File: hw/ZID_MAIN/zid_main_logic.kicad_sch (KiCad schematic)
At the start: 81 parts, among them J1 Conn_01x02_Pin_2.54mm, J2 Conn_02x05_2.54mm, J3 Conn_02x05_2.54mm, J4 Conn_02x05_PINHDR_2.54mm, J5 HDR 1x04 Socket, J6 Conn_02x03_Odd_Even, J7 Conn_01x03, M1 WS-RP2040-Zero, SW1 SW_Push, SW2 SW_DIP_x02, U1 74HCT161, U10 74FCT2245, U11 SST39SF010, U12 AS7C1024B-10J, U13 74FCT541C, U14 74AHCT244, U15 74FCT257T, U16 74HCT166, U17 74HCT166, U18 74LVC245, U19 74LVC125AS, U2 74FCT541C, U20 24LC32, U21 ATF1504AS-44T, U22 74AHCT1G125, U23 74LVC273, U25 74LVC2G04, U26 74LVC2G04-AES, U3 74FCT541C, U4 MIC2775, U6 Z80 C20MHz-PLCC, U7 ATF1508AS, U8 74FCT2245, U9 74FCT2245

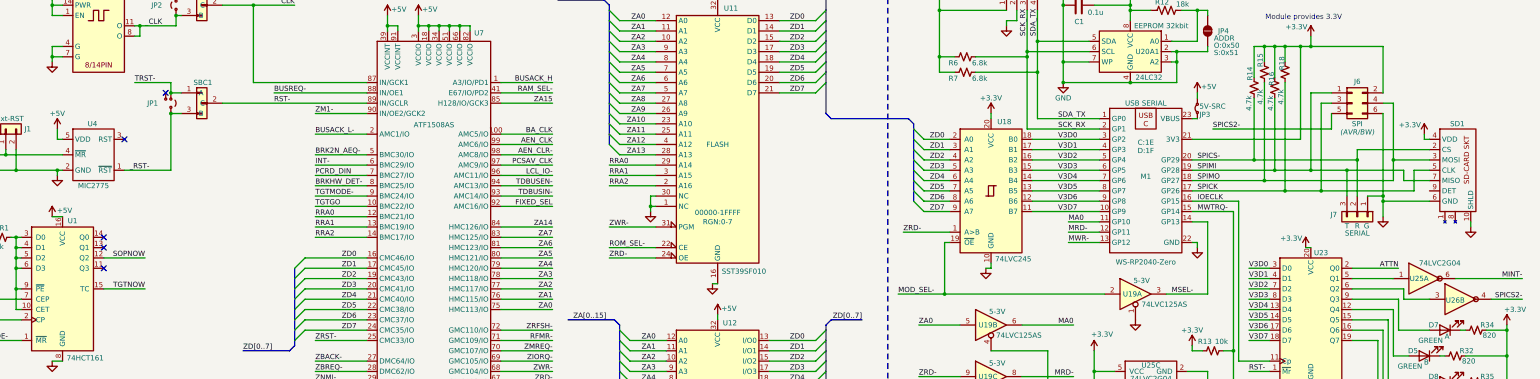
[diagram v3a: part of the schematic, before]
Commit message: Footprints assigned
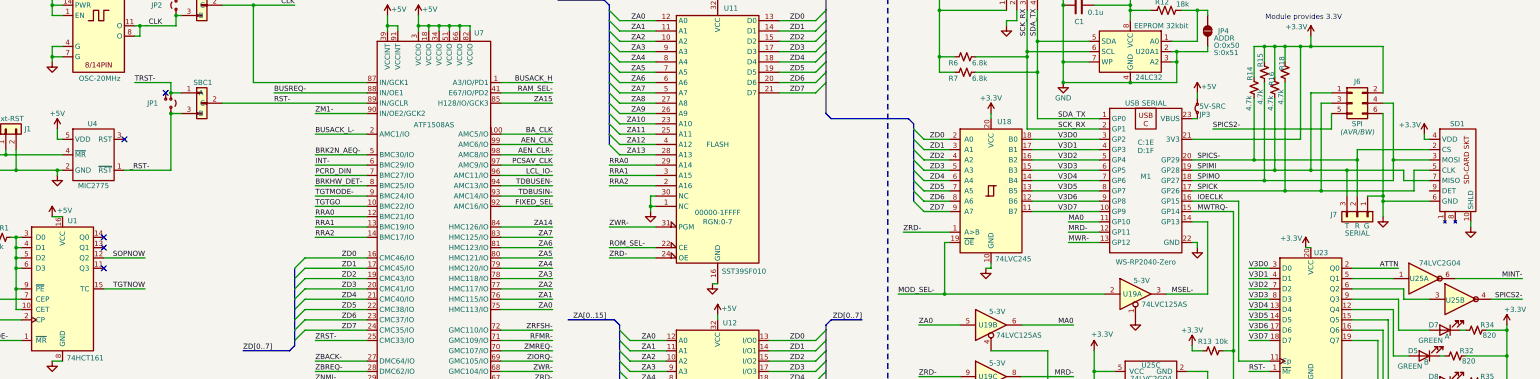
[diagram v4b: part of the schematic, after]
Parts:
- D5, D7: value LED RED -> LED GREEN; footprint LED_THT:LED_D3.0mm -> LED_SMD:LED_0805_2012Metric_Pad1.15x1.40mm_HandSolder
- D6, D8: value LED RED -> LED YELLOW; footprint LED_THT:LED_D3.0mm -> LED_SMD:LED_0805_2012Metric_Pad1.15x1.40mm_HandSolder
- D9: footprint LED_THT:LED_D3.0mm -> LED_SMD:LED_0805_2012Metric_Pad1.15x1.40mm_HandSolder
- J1: footprint (none) -> Connector_PinHeader_2.54mm:PinHeader_1x02_P2.54mm_Vertical
- J2, J3: footprint (none) -> Connector_PinHeader_2.54mm:PinHeader_2x05_P2.54mm_Vertical
- J4: footprint (none) -> Connector_IDC:IDC-Header_2x05_P2.54mm_Vertical
- J6: footprint (none) -> Connector_IDC:IDC-Header_2x03_P2.54mm_Vertical
- J7: footprint (none) -> Connector_PinHeader_2.54mm:PinHeader_1x03_P2.54mm_Vertical
- JP1: footprint (none) -> Connector_PinHeader_2.00mm:PinHeader_1x03_P2.00mm_Vertical
- JP2, JP3: footprint (none) -> Connector_PinHeader_2.00mm:PinHeader_1x02_P2.00mm_Vertical
- JP4: footprint (none) -> Jumper:SolderJumper-2_P1.3mm_Open_RoundedPad1.0x1.5mm
- R1, R4: footprint (none) -> Resistor_SMD:R_0805_2012Metric
- R12: footprint Resistor_SMD:R_0805_2012Metric_Pad1.20x1.40mm_HandSolder -> Resistor_SMD:R_0805_2012Metric
- SD1: value ~ -> SD-CARD Socket; footprint (none) -> AES_Library:AES-SDCard-GCT_MEM2075-00-140-01-A
- SW1: footprint (none) -> AES_Library:AES-SW_PUSH_SMD_1P1T_NO_6x6mm
- SW2: footprint (none) -> Button_Switch_THT:SW_DIP_SPSTx02_Piano_CTS_Series194-2MSTN_W7.62mm_P2.54mm
- TP1, TP2, TP3, TP4, TP5, TP6: footprint (none) -> Connector_PinHeader_2.54mm:PinHeader_1x01_P2.54mm_Vertical
- U1, U16, U17: footprint (none) -> Package_SO:SOIC-16_3.9x9.9mm_P1.27mm
- U10, U13, U14, U18, U2, U23, U3, U8, U9: footprint (none) -> Package_SO:SOIC-20W_7.5x12.8mm_P1.27mm
- U11: footprint (none) -> Package_DIP:DIP-32_W15.24mm_Socket_LongPads
- U15: footprint (none) -> Package_SO:SOIC-16W_7.5x10.3mm_P1.27mm
- U22: footprint (none) -> Package_TO_SOT_SMD:SOT-23-5
- U25: renamed from U26; value 74LVC2G04-AES -> 74LVC2G04
- U5: value ~ -> OSC-20MHz
- U6: footprint Package_LCC:PLCC-44 -> Package_LCC:PLCC-44_THT-Socket
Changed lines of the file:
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@@
 			)
 		)
-		(property "Footprint" ""
+		(property "Footprint" "Connector_PinHeader_2.54mm:PinHeader_1x01_P2.54mm_Vertical"
 			(at 106.68 152.4 0)
 			(effects
@@
 			)
 		)
-		(property "Footprint" ""
+		(property "Footprint" "Resistor_SMD:R_0805_2012Metric"
 			(at 30.48 78.74 0)
 			(effects
@@
 			)
 		)
-		(property "Footprint" ""
+		(property "Footprint" "Package_SO:SOIC-20W_7.5x12.8mm_P1.27mm"
 			(at 142.24 201.93 0)
 			(effects
@@
 			)
 		)
-		(property "Footprint" ""
+		(property "Footprint" "Connector_PinHeader_2.54mm:PinHeader_1x03_P2.54mm_Vertical"
 			(at 364.49 73.66 0)
 			(effects
@@
 			)
 		)
-		(property "Footprint" "Package_LCC:PLCC-44"
+		(property "Footprint" "Package_LCC:PLCC-44_THT-Socket"
 			(at 71.12 282.448 0)
 			(effects
@@
 			)
 		)
-		(property "Footprint" ""
+		(property "Footprint" "Package_SO:SOIC-20W_7.5x12.8mm_P1.27mm"
 			(at 45.72 179.07 0)
 			(effects
@@
 			)
 		)
-		(property "Footprint" ""
+		(property "Footprint" "Connector_PinHeader_2.54mm:PinHeader_1x02_P2.54mm_Vertical"
 			(at 31.75 52.07 0)
 			(effects
@@
 			)
 		)
-		(property "Value" "LED RED"
+		(property "Value" "LED GREEN"
 			(at 380.746 105.664 0)
 			(effects
@@
 			)
 		)
-		(property "Footprint" "LED_THT:LED_D3.0mm"
+		(property "Footprint" "LED_SMD:LED_0805_2012Metric_Pad1.15x1.40mm_HandSolder"
 			(at 381 107.95 0)
 			(effects
@@
 			)
 		)
-		(property "Footprint" ""
+		(property "Footprint" "Button_Switch_THT:SW_DIP_SPSTx02_Piano_CTS_Series194-2MSTN_W7.62mm_P2.54mm"
 			(at 30.48 300.99 0)
 			(effects
@@
 			)
 		)
-		(property "Value" "LED RED"
+		(property "Value" "LED YELLOW"
 			(at 385.826 112.014 0)
 			(effects
@@
 			)
 		)
-		(property "Footprint" "LED_THT:LED_D3.0mm"
+		(property "Footprint" "LED_SMD:LED_0805_2012Metric_Pad1.15x1.40mm_HandSolder"
 			(at 386.08 114.3 0)
 			(effects
@@
 			)
 		)
-		(property "Footprint" ""
+		(property "Footprint" "Connector_PinHeader_2.54mm:PinHeader_2x05_P2.54mm_Vertical"
 			(at 171.45 285.75 0)
 			(effects
@@
 			)
 		)
-		(property "Footprint" ""
+		(property "Footprint" "Connector_IDC:IDC-Header_2x03_P2.54mm_Vertical"
 			(at 363.22 45.72 0)
 			(effects
@@
 			)
 		)
-		(property "Footprint" ""
+		(property "Footprint" "Package_SO:SOIC-16W_7.5x10.3mm_P1.27mm"
 			(at 210.82 185.42 0)
 			(effects
@@
 			)
 		)
-		(property "Value" "LED RED"
+		(property "Value" "LED GREEN"
 			(at 385.826 99.314 0)
 			(effects
@@
 			)
 		)
-		(property "Footprint" "LED_THT:LED_D3.0mm"
+		(property "Footprint" "LED_SMD:LED_0805_2012Metric_Pad1.15x1.40mm_HandSolder"
 			(at 386.08 101.6 0)
 			(effects
@@
 		(on_board yes)
 		(dnp no)
-		(property "Reference" "U26"
+		(property "Reference" "U25"
 			(at 388.62 94.234 0)
 			(effects
@@
 			)
 		)
-		(property "Value" "74LVC2G04-AES"
+		(property "Value" "74LVC2G04"
 			(at 388.62 95.25 0)
 			(effects
@@
 			(project ""
 				(path "/2be47242-6db6-4d8d-b590-8c682dee013e/f092485f-e7d4-42be-add8-9bafec004ccb"
-					(reference "U26")
+					(reference "U25")
 					(unit 2)
 				)
@@
 			)
 		)
-		(property "Footprint" ""
+		(property "Footprint" "Connector_IDC:IDC-Header_2x05_P2.54mm_Vertical"
 			(at 259.08 170.18 0)
 			(effects
@@
 			)
 		)
-		(property "Footprint" "Resistor_SMD:R_0805_2012Metric_Pad1.20x1.40mm_HandSolder"
+		(property "Footprint" "Resistor_SMD:R_0805_2012Metric"
 			(at 317.754 21.844 90)
 			(effects
@@
 			)
 		)
-		(property "Footprint" ""
+		(property "Footprint" "Package_DIP:DIP-32_W15.24mm_Socket_LongPads"
 			(at 207.01 48.26 0)
 			(effects
@@
 			)
 		)
-		(property "Value" "~"
-			(at 54.61 31.496 0)
+		(property "Value" "OSC-20MHz"
+			(at 54.864 39.624 0)
 			(effects
 				(font
@@
 			)
 		)
-		(property "Footprint" ""
+		(property "Footprint" "Connector_PinHeader_2.54mm:PinHeader_1x01_P2.54mm_Vertical"
 			(at 171.45 111.76 0)
 			(effects
@@
 			)
 		)
-		(property "Footprint" ""
+		(property "Footprint" "Connector_PinHeader_2.00mm:PinHeader_1x03_P2.00mm_Vertical"
 			(at 72.39 45.72 0)
 			(effects
@@
 			)
 		)
-		(property "Footprint" ""
+		(property "Footprint" "Package_SO:SOIC-20W_7.5x12.8mm_P1.27mm"
 			(at 209.55 240.03 0)
 			(effects
@@
 			)
 		)
-		(property "Footprint" ""
+		(property "Footprint" "Package_TO_SOT_SMD:SOT-23-5"
 			(at 328.93 163.83 0)
 			(effects
@@
 			)
 		)
-		(property "Footprint" ""
+		(property "Footprint" "Connector_PinHeader_2.00mm:PinHeader_1x02_P2.00mm_Vertical"
 			(at 325.12 46.99 0)
 			(effects
@@
 			)
 		)
-		(property "Footprint" ""
+		(property "Footprint" "Connector_PinHeader_2.54mm:PinHeader_1x01_P2.54mm_Vertical"
 			(at 355.6 163.83 0)
 			(effects
@@
 			)
 		)
-		(property "Footprint" ""
+		(property "Footprint" "Package_SO:SOIC-16_3.9x9.9mm_P1.27mm"
 			(at 271.78 224.79 0)
 			(effects
@@
 			)
 		)
-		(property "Footprint" ""
+		(property "Footprint" "Package_SO:SOIC-20W_7.5x12.8mm_P1.27mm"
 			(at 207.01 285.75 0)
 			(effects
@@
 			)
 		)
-		(property "Value" "~"
+		(property "Value" "SD-CARD Socket"
 			(at 389.89 62.23 0)
 			(effects
@@
 			)
 		)
-		(property "Footprint" ""
+		(property "Footprint" "AES_Library:AES-SDCard-GCT_MEM2075-00-140-01-A"
 			(at 389.89 62.23 0)
 			(effects
@@
 			)
 		)
-		(property "Footprint" "LED_THT:LED_D3.0mm"
+		(property "Footprint" "LED_SMD:LED_0805_2012Metric_Pad1.15x1.40mm_HandSolder"
 			(at 386.08 127 0)
 			(effects
@@
 			)
 		)
-		(property "Footprint" ""
+		(property "Footprint" "Connector_PinHeader_2.54mm:PinHeader_2x05_P2.54mm_Vertical"
 			(at 238.76 275.59 0)
 			(effects
@@
 			)
 		)
-		(property "Footprint" ""
+		(property "Footprint" "Connector_PinHeader_2.54mm:PinHeader_1x01_P2.54mm_Vertical"
 			(at 290.83 215.9 0)
 			(effects
@@
 			)
 		)
-		(property "Footprint" ""
+		(property "Footprint" "Package_SO:SOIC-16_3.9x9.9mm_P1.27mm"
 			(at 45.72 91.44 0)
 			(effects
@@
 			)
 		)
-		(property "Value" "LED RED"
+		(property "Value" "LED YELLOW"
 			(at 380.746 118.364 0)
 			(effects
@@
 			)
 		)
-		(property "Footprint" "LED_THT:LED_D3.0mm"
+		(property "Footprint" "LED_SMD:LED_0805_2012Metric_Pad1.15x1.40mm_HandSolder"
 			(at 381 120.65 0)
 			(effects
@@
 			)
 		)
-		(property "Footprint" ""
+		(property "Footprint" "Package_SO:SOIC-20W_7.5x12.8mm_P1.27mm"
 			(at 274.32 67.31 0)
 			(effects
@@
 			)
 		)
-		(property "Footprint" ""
+		(property "Footprint" "Package_SO:SOIC-20W_7.5x12.8mm_P1.27mm"
 			(at 45.72 137.16 0)
 			(effects
@@
 			)
 		)
-		(property "Footprint" ""
+		(property "Footprint" "Resistor_SMD:R_0805_2012Metric"
 			(at 93.98 135.89 0)
 			(effects
@@
 			)
 		)
-		(property "Footprint" ""
+		(property "Footprint" "Package_SO:SOIC-20W_7.5x12.8mm_P1.27mm"
 			(at 353.06 99.06 0)
 			(effects
@@
 			)
 		)
-		(property "Footprint" ""
+		(property "Footprint" "AES_Library:AES-SW_PUSH_SMD_1P1T_NO_6x6mm"
 			(at 22.86 53.34 0)
 			(effects
@@
 			)
 		)
-		(property "Footprint" ""
+		(property "Footprint" "Connector_PinHeader_2.54mm:PinHeader_1x01_P2.54mm_Vertical"
 			(at 290.83 218.44 0)
 			(effects
@@
 			)
 		)
-		(property "Footprint" ""
+		(property "Footprint" "Package_SO:SOIC-20W_7.5x12.8mm_P1.27mm"
 			(at 142.24 285.75 0)
 			(effects
@@
 			)
 		)
-		(property "Footprint" ""
+		(property "Footprint" "Jumper:SolderJumper-2_P1.3mm_Open_RoundedPad1.0x1.5mm"
 			(at 327.66 27.94 0)
 			(effects
@@
 			)
 		)
-		(property "Footprint" ""
+		(property "Footprint" "Connector_PinHeader_2.54mm:PinHeader_1x01_P2.54mm_Vertical"
 			(at 171.45 116.84 0)
 			(effects
@@
 			)
 		)
-		(property "Footprint" ""
+		(property "Footprint" "Package_SO:SOIC-16_3.9x9.9mm_P1.27mm"
 			(at 271.78 281.94 0)
 			(effects
@@
 			)
 		)
-		(property "Footprint" ""
+		(property "Footprint" "Connector_PinHeader_2.00mm:PinHeader_1x02_P2.00mm_Vertical"
 			(at 73.66 21.59 0)
 			(effects
@@
 			)
 		)
-		(property "Footprint" ""
+		(property "Footprint" "Package_SO:SOIC-20W_7.5x12.8mm_P1.27mm"
 			(at 142.24 243.84 0)
 			(effects

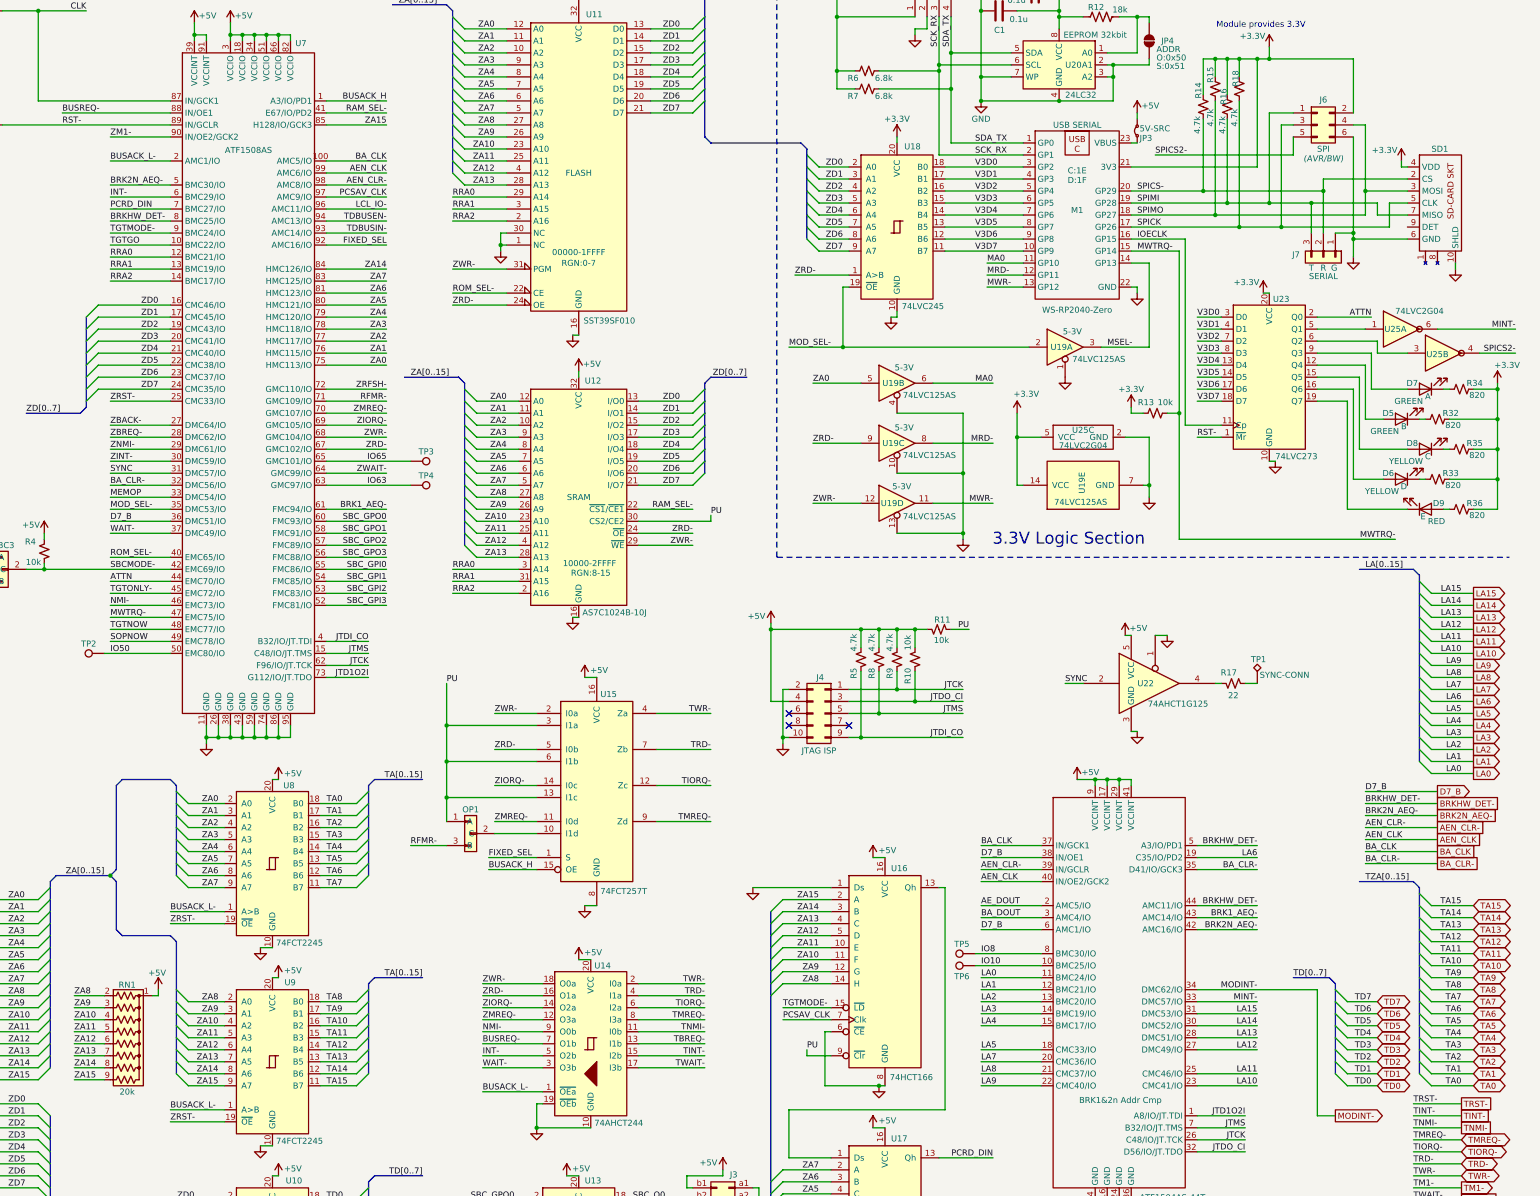
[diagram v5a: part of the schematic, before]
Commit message: 74LVC3G04, free up BUSACK_H and BUSACK_L.
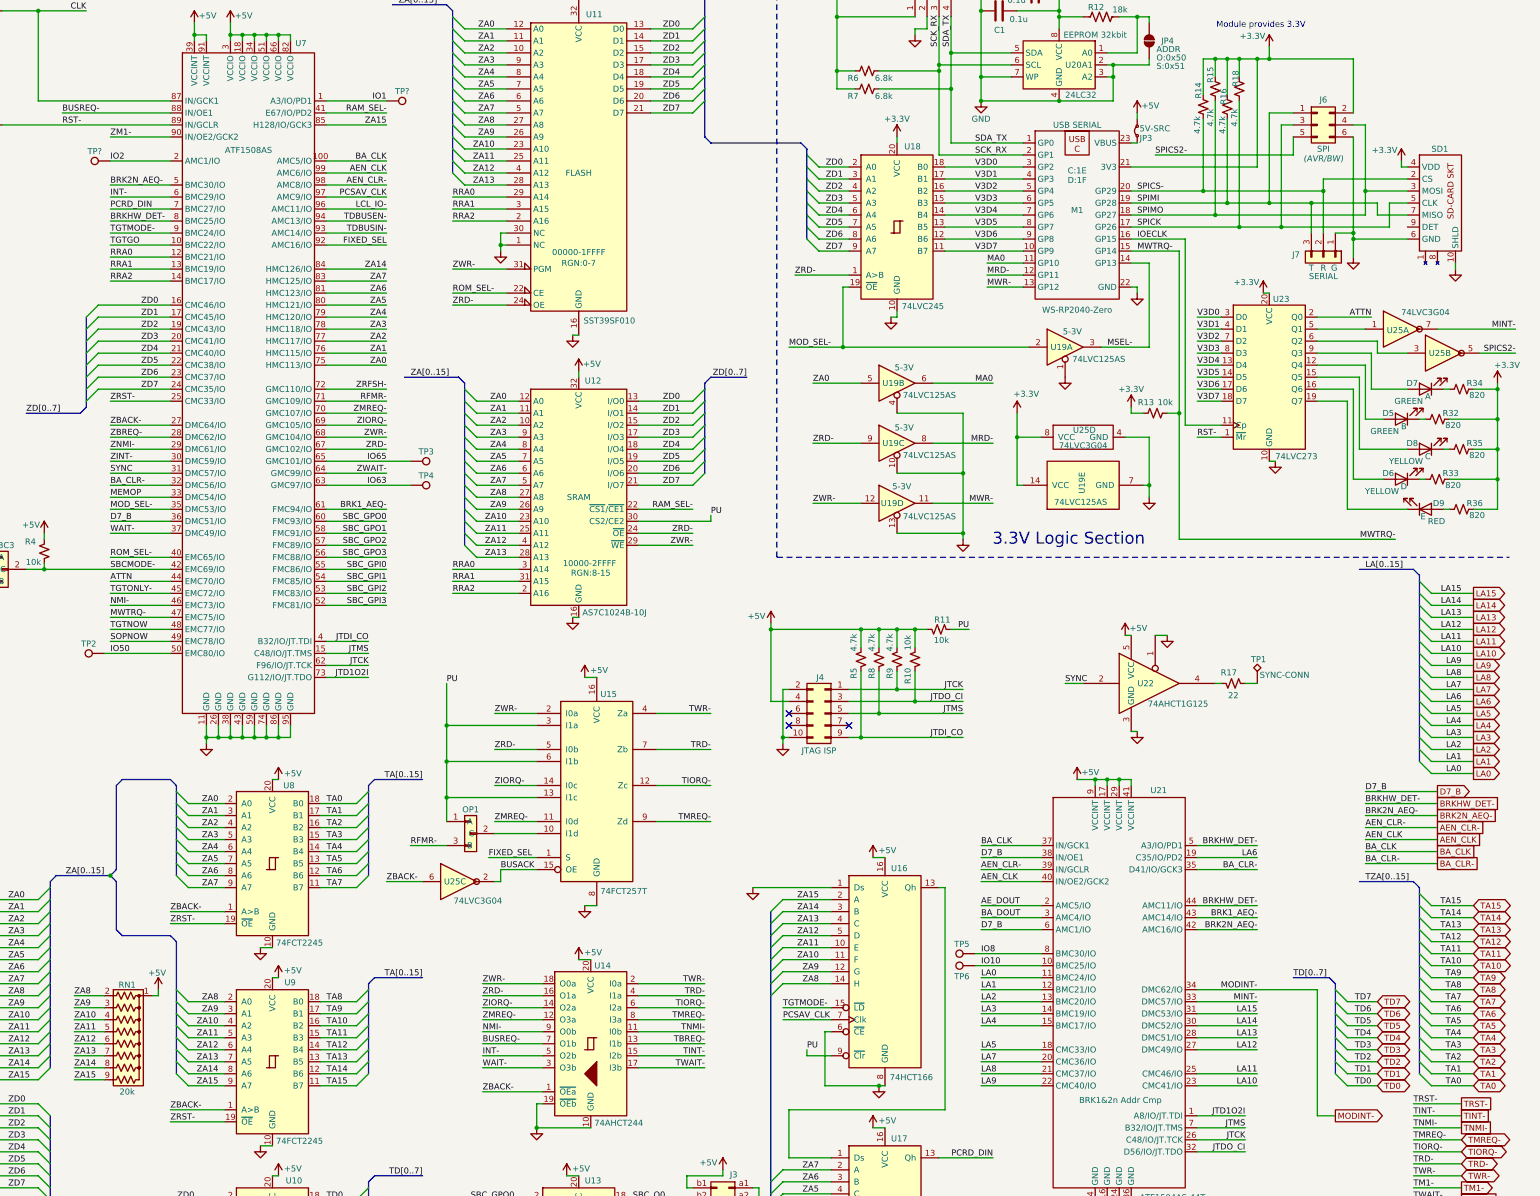
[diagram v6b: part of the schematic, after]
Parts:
- removed U25: 74LVC2G04, Package_TO_SOT_SMD:SOT-23-6, symbol AES_Library:74LVC2G04-AES
- added TP? (x2): TestPoint, Connector_PinHeader_2.54mm:PinHeader_1x01_P2.54mm_Vertical, symbol Connector:TestPoint
- added U25: 74LVC3G04, Package_SO:SSOP-8_2.95x2.8mm_P0.65mm, symbol AES_Library:74LVC3G04-AES
- J2, J3: footprint Connector_PinHeader_2.54mm:PinHeader_2x05_P2.54mm_Vertical -> AES_Library:PinHeader_2x05_AB-AES
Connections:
- net +3.3V: now also U25.8 (VCC)
- net GND: now also U25.4 (GND)
- net MINT-: now also U25.7
- net SPICS2-: now also U25.5
- net ZBACK-: now also U14.1 (~{OEa}), U8.1 (A>B), U9.1 (A>B), U25.6
- net at U23.5 (Q1): now also U25.1
- net at U23.6 (Q2): now also U25.3
- net BUSACK_H renamed BUSACK
- net BUSACK: now also U25.2; no longer U7.1 (A3/IO/PD1)
- removed net BUSACK_L-: U14.1 (~{OEa}), U7.2 (AMC1/IO), U8.1 (A>B), U9.1 (A>B)
- new net IO1: TP?.1, U7.1 (A3/IO/PD1)
- new net IO2: TP?.1, U7.2 (AMC1/IO)
